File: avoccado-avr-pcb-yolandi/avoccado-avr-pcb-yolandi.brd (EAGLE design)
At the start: 50 x 49 mm, 49 parts, among them Q1 16MHz, Q2 FET, U2 MCP73831

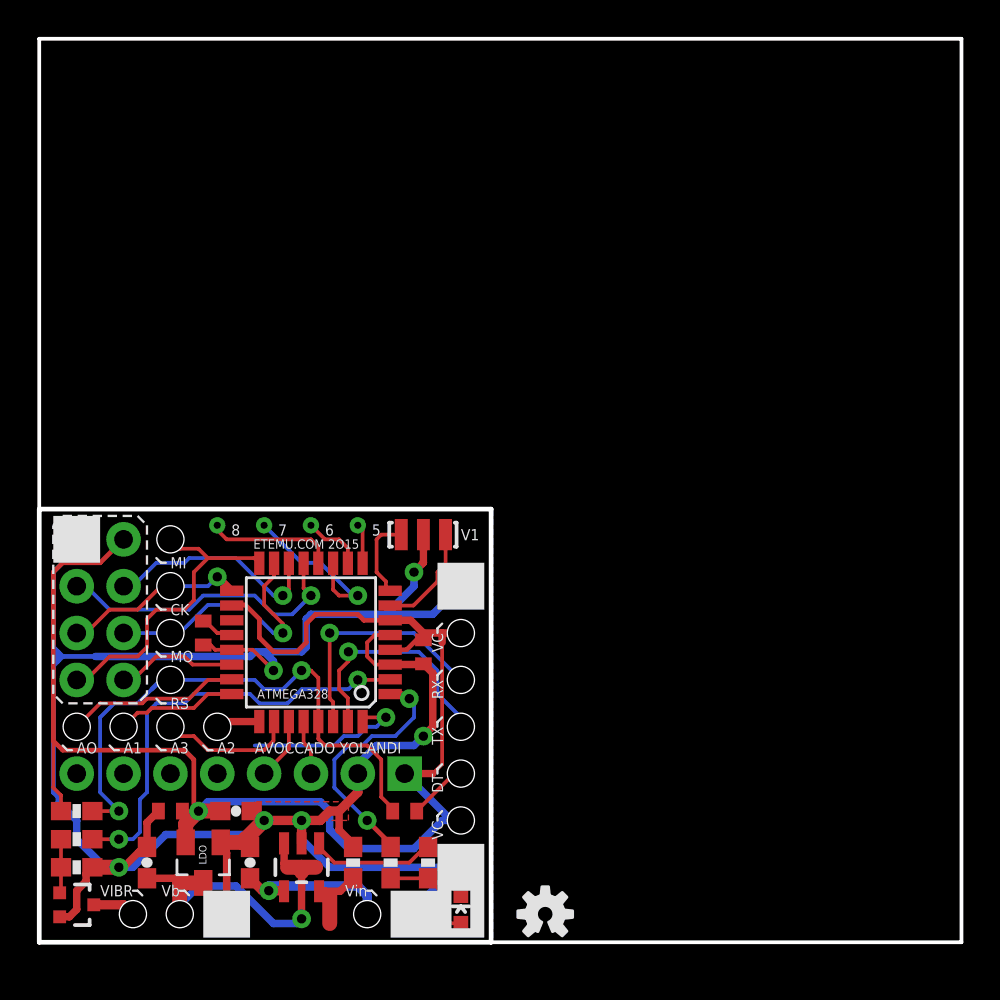
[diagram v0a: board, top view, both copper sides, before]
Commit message: bottom silkscreen
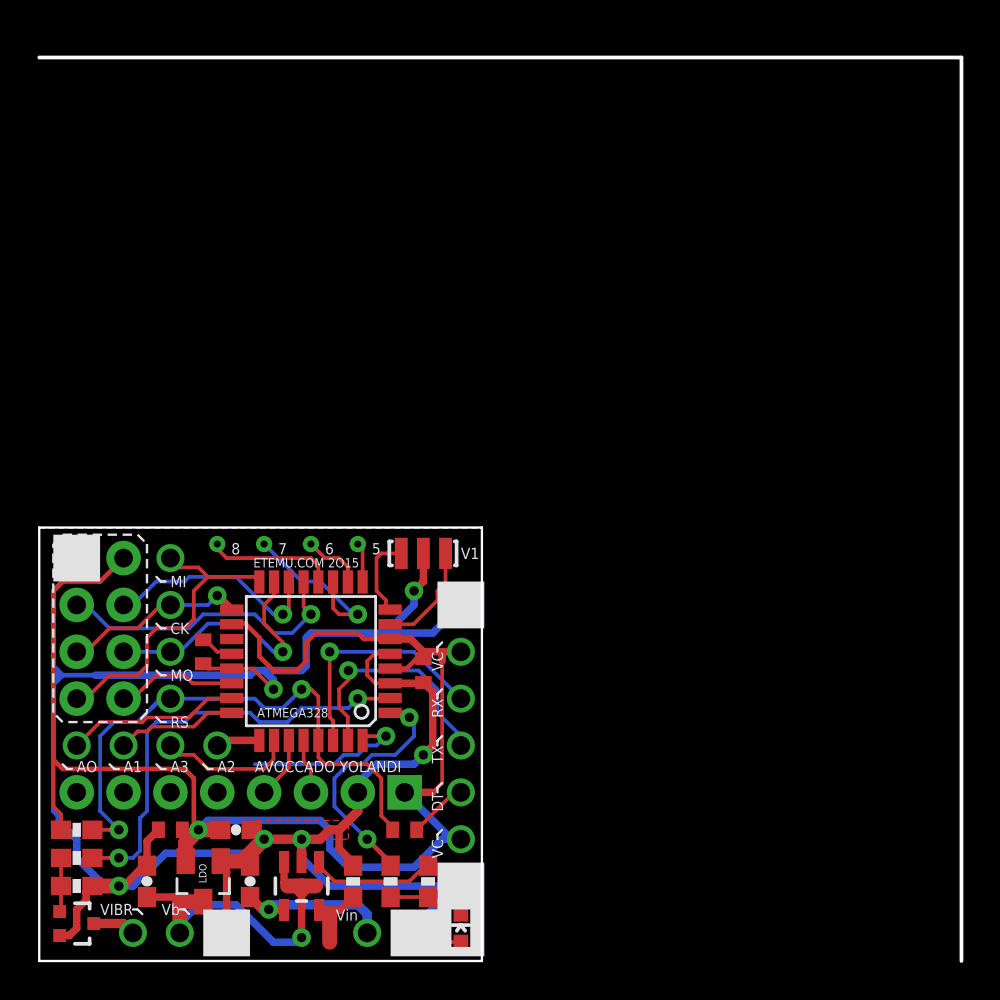
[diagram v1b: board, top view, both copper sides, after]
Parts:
- JP10, JP11, JP12, JP13, JP14, JP15, JP17, JP18, JP19, JP20, JP21, JP22, JP23, JP24, JP25, JP26, JP3, JP6, JP8, JP9: value M01POGOPIN_HOLE_0.58 -> M01NOSILK-KIT; device SparkFun-Connectors:1X01_POGOPIN_HOLE_0.58 -> SparkFun-Connectors:1X01NS-KIT
- moved LOGO1 25.2 mm to (2.29, 2.03), flipped to the bottom
- moved C1 1.02 mm to (8.89, 16.8)
- moved JP11 1.02 mm to (22.9, 16.8)
- moved JP13 1.02 mm to (7.11, 19.3)
- moved JP14 1.02 mm to (7.11, 16.8)
- moved JP27 1.02 mm to (2.03, 19.3)
- moved JP28 1.02 mm to (2.03, 16.8)
- moved JP3 1.02 mm to (22.9, 19.3)
- moved Q1 1.02 mm to (20.8, 22.1)
- moved C10 1.02 mm to (7.11, 7.11)
- moved C2 1.02 mm to (19.8, 7.11)
- moved C3 1.02 mm to (20.8, 15.7)
- moved C4 1.02 mm to (11.4, 4.32)
- moved C5 1.02 mm to (5.84, 4.32)
- moved C6 1.02 mm to (10.7, 7.11)
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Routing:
- net GND: track 126.2 -> 127.7 mm
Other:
- outline, holes or cut-outs redrawn
- board text added: "ATTENZIONE! DO NOT SWALLOW THIS PRODUCT"
- board text added: "MPU6050"
- board text added: "NRF24L01+"
- board text added: "SHURE OPEN TECHNOLOGIES AVOCCADO AVR YOLANDI V1 ETEMU.COM 2014"

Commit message: shrink dimensions 1mm
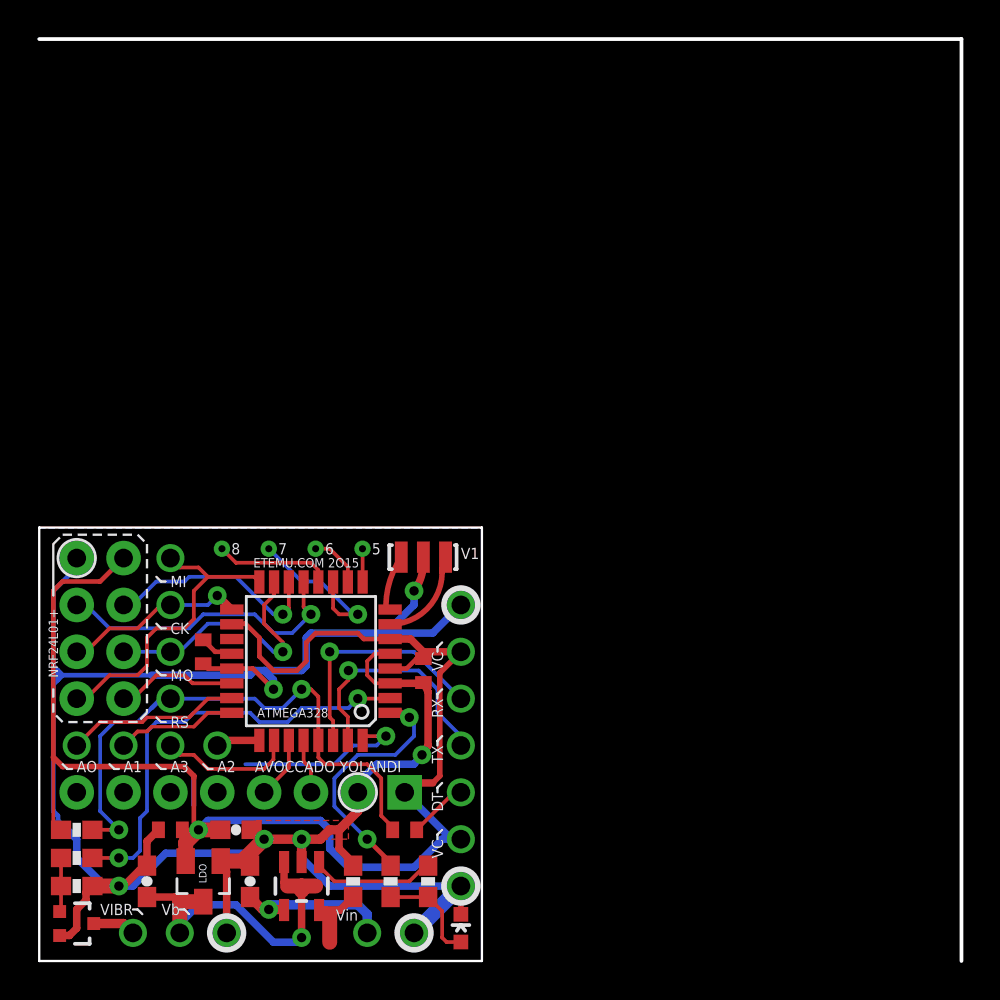
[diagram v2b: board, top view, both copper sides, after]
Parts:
- moved TP1 0.36 mm to (17.5, 22.4)
- moved TP6 0.36 mm to (15.0, 22.4)
- moved TP8 0.36 mm to (9.91, 22.4)
- moved TP7 0.36 mm to (12.4, 22.4)
- moved Q1 0.20 mm to (20.8, 21.9)
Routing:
- net N$1: track 4.54 -> 2.74 mm
- net N$2: track 5.83 -> 4.88 mm
- net D8: track 7.01 -> 6.35 mm
- net GND: track 127.7 -> 127.1 mm
- net D2: track 9.10 -> 9.61 mm
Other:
- board size 50 x 49 mm -> 50 x 50 mm

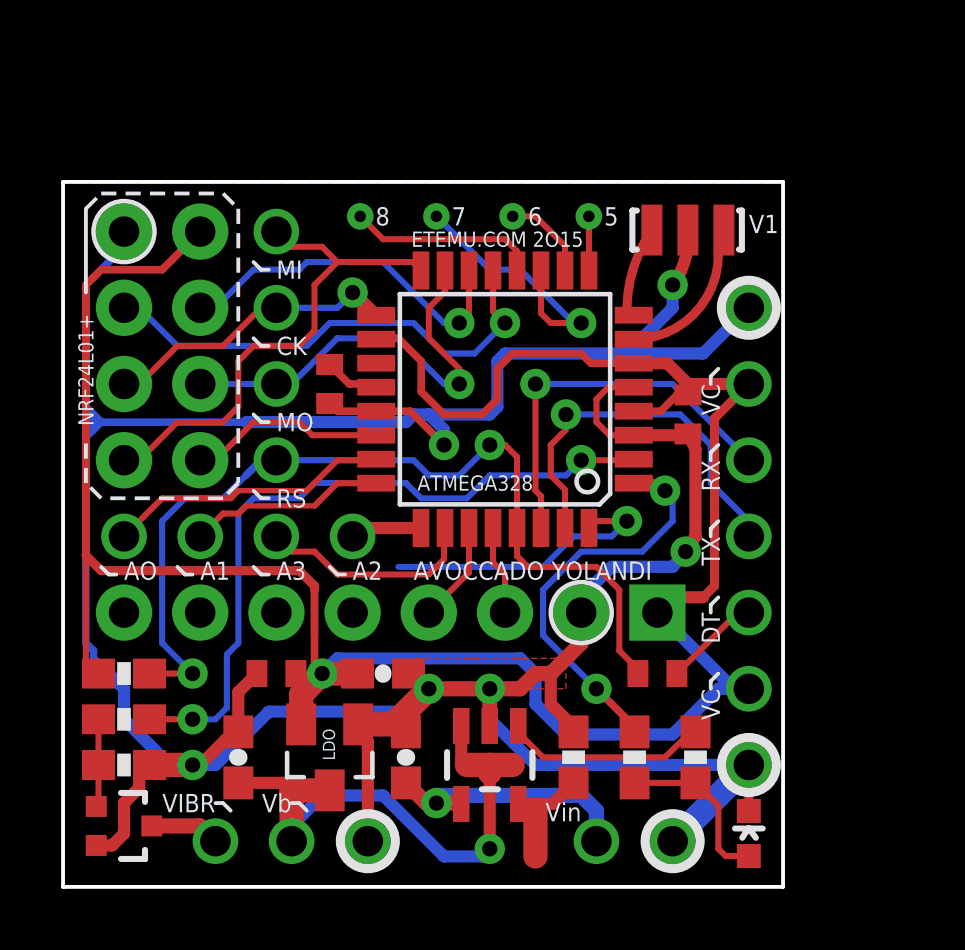
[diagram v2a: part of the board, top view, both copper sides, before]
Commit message: clear silkscreen which is outside of dimension layer
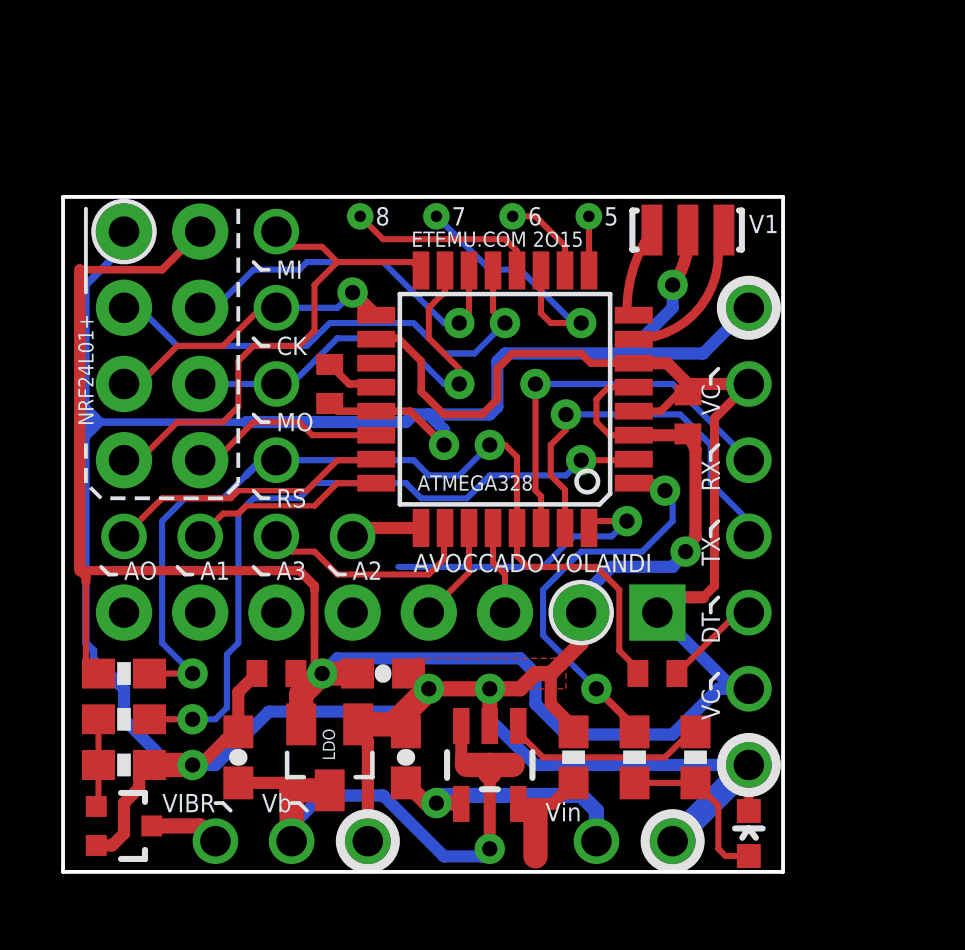
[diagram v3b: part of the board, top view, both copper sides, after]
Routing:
- net 3.3V: track 81.6 -> 82.1 mm
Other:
- outline, holes or cut-outs redrawn
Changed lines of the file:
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@@
 <setting verticaltext="up"/>
 </settings>
-<grid distance="0.02" unitdist="inch" unit="inch" style="lines" multiple="1" display="yes" altdistance="0.01" altunitdist="inch" altunit="inch"/>
+<grid distance="1" unitdist="mm" unit="mm" style="lines" multiple="1" display="yes" altdistance="0.5" altunitdist="mm" altunit="mm"/>
 <layers>
 <layer number="1" name="Top" color="4" fill="1" visible="yes" active="yes"/>
@@
 <circle x="17.526" y="22.352" radius="0.2032" width="0.4064" layer="29"/>
 <text x="11.6078" y="21.336" size="0.508" layer="21" font="vector">ETEMU.COM 2O15</text>
-<text x="11.684" y="10.541" size="0.6096" layer="21" font="vector" align="center-left">AVOCCADO YOLANDI</text>
+<text x="11.684" y="10.795" size="0.6096" layer="21" font="vector" align="center-left">AVOCCADO YOLANDI</text>
 <text x="7.112" y="12.954" size="0.6096" layer="21" ratio="10" rot="SR0" align="center-left">RS</text>
 <wire x1="6.858" y1="12.954" x2="6.604" y2="12.954" width="0.127" layer="21"/>
@@
 <wire x1="0.762" y1="13.462" x2="0.762" y2="14.986" width="0.127" layer="21" style="shortdash"/>
 <wire x1="0.762" y1="19.812" x2="0.762" y2="22.606" width="0.127" layer="21"/>
-<wire x1="0.762" y1="22.606" x2="1.27" y2="23.114" width="0.127" layer="21" style="shortdash"/>
-<wire x1="1.27" y1="23.114" x2="5.334" y2="23.114" width="0.127" layer="21" style="shortdash"/>
-<wire x1="5.334" y1="23.114" x2="5.842" y2="22.606" width="0.127" layer="21" style="shortdash"/>
-<wire x1="0" y1="0" x2="24" y2="0" width="0.127" layer="20"/>
-<wire x1="24" y1="0" x2="24" y2="23.5" width="0.127" layer="20"/>
-<wire x1="24" y1="23.5" x2="0" y2="23.5" width="0.127" layer="20"/>
-<wire x1="0" y1="23.5" x2="0" y2="0" width="0.127" layer="20"/>
+<wire x1="0" y1="0.5" x2="24" y2="0.5" width="0.127" layer="20"/>
+<wire x1="24" y1="0.5" x2="24" y2="23" width="0.127" layer="20"/>
+<wire x1="24" y1="23" x2="0" y2="23" width="0.127" layer="20"/>
+<wire x1="0" y1="23" x2="0" y2="0.5" width="0.127" layer="20"/>
 <text x="23.368" y="22.733" size="0.6096" layer="22" font="vector" rot="MR0" align="top-left">ATTENZIONE!
 DO NOT SWALLOW THIS PRODUCT</text>
@@
 ETEMU.COM 2014</text>
 <text x="0.762" y="21.209" size="0.508" layer="22" font="vector" rot="MR270" align="center-left">NRF24L01+</text>
-<wire x1="1.27" y1="23.114" x2="5.334" y2="23.114" width="0.127" layer="22" style="longdash"/>
-<wire x1="5.334" y1="23.114" x2="5.842" y2="22.606" width="0.127" layer="22" style="longdash"/>
 <wire x1="5.842" y1="22.606" x2="5.842" y2="13.462" width="0.127" layer="22" style="longdash"/>
 <wire x1="5.842" y1="13.462" x2="5.334" y2="12.954" width="0.127" layer="22" style="longdash"/>
@@
 <wire x1="1.27" y1="12.954" x2="0.762" y2="13.462" width="0.127" layer="22" style="longdash"/>
 <wire x1="0.762" y1="13.462" x2="0.762" y2="16.764" width="0.127" layer="22" style="longdash"/>
-<wire x1="1.27" y1="23.114" x2="0.762" y2="22.606" width="0.127" layer="22" style="longdash"/>
 <wire x1="0.762" y1="22.606" x2="0.762" y2="21.336" width="0.127" layer="22" style="longdash"/>
 <wire x1="1.27" y1="10.414" x2="0.762" y2="9.906" width="0.127" layer="22" style="longdash"/>
@@
 <contactref element="AVR" pad="3"/>
 <contactref element="AVR" pad="5"/>
-<polygon width="0.254" layer="16" isolate="0.254">
-<vertex x="0" y="23.458"/>
-<vertex x="23.988" y="23.458"/>
-<vertex x="23.988" y="0"/>
-<vertex x="0" y="0"/>
+<polygon width="0.2032" layer="16" isolate="0.3048">
+<vertex x="0" y="22.958"/>
+<vertex x="23.988" y="22.958"/>
+<vertex x="23.988" y="0.5"/>
+<vertex x="0" y="0.5"/>
 </polygon>
 <contactref element="LDO" pad="1"/>
@@
 <wire x1="21.717" y1="10.033" x2="21.717" y2="15.621" width="0.3048" layer="1"/>
 <wire x1="4.572" y1="21.844" x2="3.302" y2="20.574" width="0.254" layer="1"/>
-<wire x1="3.302" y1="20.574" x2="1.27" y2="20.574" width="0.254" layer="1"/>
-<wire x1="1.27" y1="20.574" x2="0.762" y2="20.066" width="0.254" layer="1"/>
-<wire x1="0.762" y1="20.066" x2="0.762" y2="11.049" width="0.254" layer="1"/>
+<wire x1="3.302" y1="20.574" x2="0.5588" y2="20.574" width="0.254" layer="1"/>
+<wire x1="0.5588" y1="20.574" x2="0.5588" y2="10.541" width="0.381" layer="1"/>
 <contactref element="C6" pad="1"/>
-<wire x1="0.762" y1="11.049" x2="0.762" y2="10.922" width="0.254" layer="1"/>
 <wire x1="19.812" y1="9.144" x2="22.352" y2="6.604" width="0.4064" layer="16"/>
 <wire x1="22.352" y1="6.604" x2="22.86" y2="6.604" width="0.4064" layer="16"/>
@@
 <wire x1="8.636" y1="7.112" x2="8.382" y2="7.366" width="0.254" layer="1"/>
 <wire x1="8.382" y1="7.366" x2="8.382" y2="9.906" width="0.254" layer="1"/>
-<wire x1="7.874" y1="10.541" x2="1.27" y2="10.541" width="0.3048" layer="1"/>
+<wire x1="7.874" y1="10.541" x2="0.5588" y2="10.541" width="0.3048" layer="1"/>
 <wire x1="7.94" y1="5.418" x2="7.94" y2="6.416" width="0.8128" layer="1"/>
 <wire x1="7.94" y1="6.416" x2="8.636" y2="7.112" width="0.8128" layer="1"/>
 <wire x1="9.818" y1="7.112" x2="8.636" y2="7.112" width="0.8128" layer="1"/>
-<wire x1="0.762" y1="7.532" x2="0.762" y2="10.922" width="0.2032" layer="1"/>
+<wire x1="0.762" y1="7.532" x2="0.762" y2="10.16" width="0.2032" layer="1"/>
 <contactref element="JP2" pad="2"/>
 <wire x1="7.762" y1="7.112" x2="8.636" y2="7.112" width="0.2032" layer="1"/>
 <wire x1="8.382" y1="9.906" x2="8.382" y2="10.033" width="0.3048" layer="1"/>
 <wire x1="8.382" y1="10.033" x2="7.874" y2="10.541" width="0.3048" layer="1"/>
-<wire x1="1.27" y1="10.541" x2="0.762" y2="11.049" width="0.3048" layer="1"/>
 <wire x1="0.762" y1="7.532" x2="1.182" y2="7.112" width="0.2032" layer="1"/>
 <wire x1="21.717" y1="15.621" x2="22.86" y2="16.764" width="0.3048" layer="1"/>
@@
 <wire x1="21.336" y1="9.652" x2="20.32" y2="9.652" width="0.4064" layer="1"/>
 <wire x1="20.32" y1="9.652" x2="19.812" y2="9.144" width="0.3048" layer="1"/>
+<wire x1="0.762" y1="10.16" x2="0.762" y2="10.3378" width="0.3048" layer="1"/>
+<wire x1="0.762" y1="10.3378" x2="0.5588" y2="10.541" width="0.3048" layer="1"/>
 </signal>
 <signal name="D9">

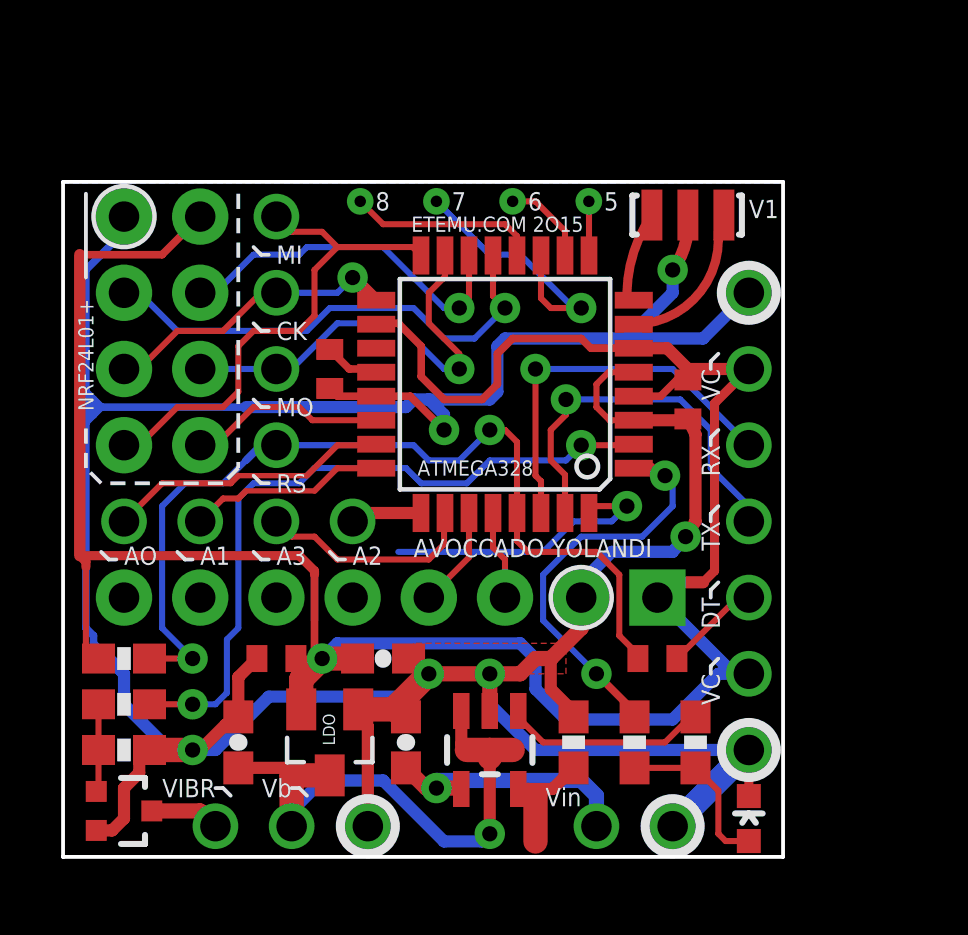
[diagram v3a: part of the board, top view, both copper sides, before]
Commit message: silkscreen component values
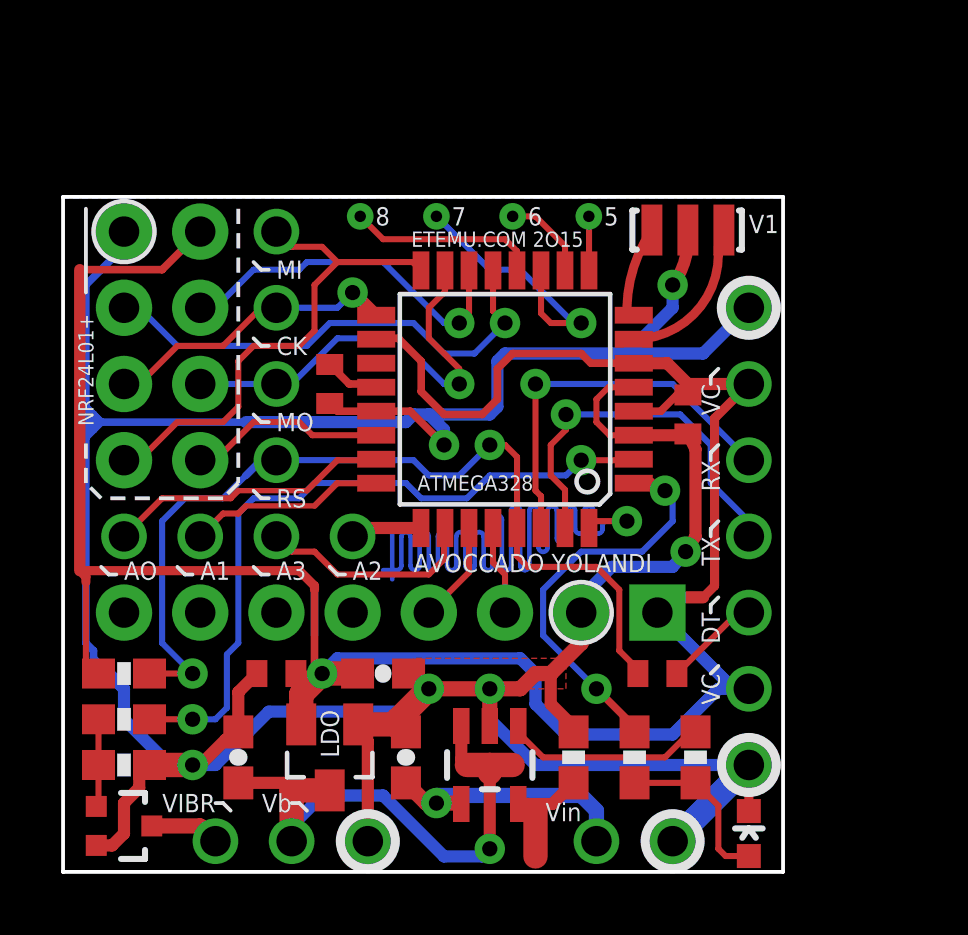
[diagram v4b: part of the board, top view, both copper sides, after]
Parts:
- R3: value 2K -> Rchg
- moved AVR 0.50 mm to (14.7, 15.8)
- moved C1 0.50 mm to (8.89, 16.3)
- moved C10 0.50 mm to (7.11, 6.61)
- moved C2 0.50 mm to (19.8, 6.61)
- moved C3 0.50 mm to (20.8, 15.2)
- moved C6 0.50 mm to (10.7, 6.61)
- moved D1 0.50 mm to (22.9, 1.28)
- moved JP1 0.50 mm to (19.8, 8.64)
- moved JP10 0.50 mm to (22.9, 8.64)
- moved JP11 0.50 mm to (22.9, 16.3)
- moved JP12 0.50 mm to (7.11, 21.3)
- moved JP13 0.50 mm to (7.11, 18.8)
- moved JP14 0.50 mm to (7.11, 16.3)
- moved JP15 0.50 mm to (7.11, 13.7)
- moved JP17 0.50 mm to (17.8, 1.02)
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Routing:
- net D2: track 9.61 -> 38.6 mm
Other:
- outline, holes or cut-outs redrawn
- board text added: "+"
- board text added: "-"
- board text added: "WARNING - DO NOT SWALLOW THIS PRODUCT"
- board text removed: "ATTENZIONE! DO NOT SWALLOW THIS PRODUCT"
